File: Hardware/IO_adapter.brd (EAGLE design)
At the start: 67.3 x 41.9 mm, 23 parts, among them Y1 32Khz

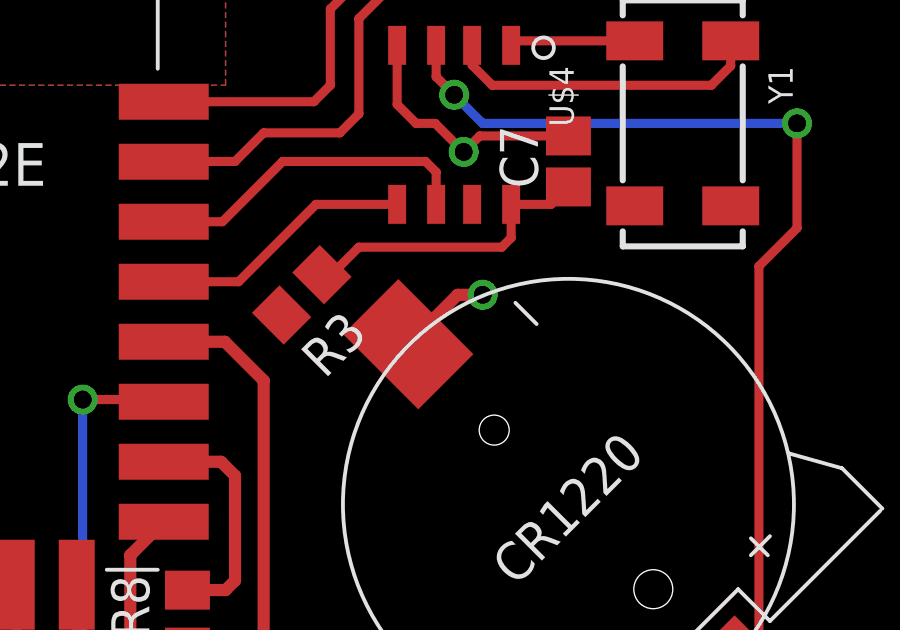
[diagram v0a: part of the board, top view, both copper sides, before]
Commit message: Revert "beginning to add a 2.2" TFT display"
This reverts commit 5a3055f75d7c66bfc0e3a1cc9d4d5180e17e1807.
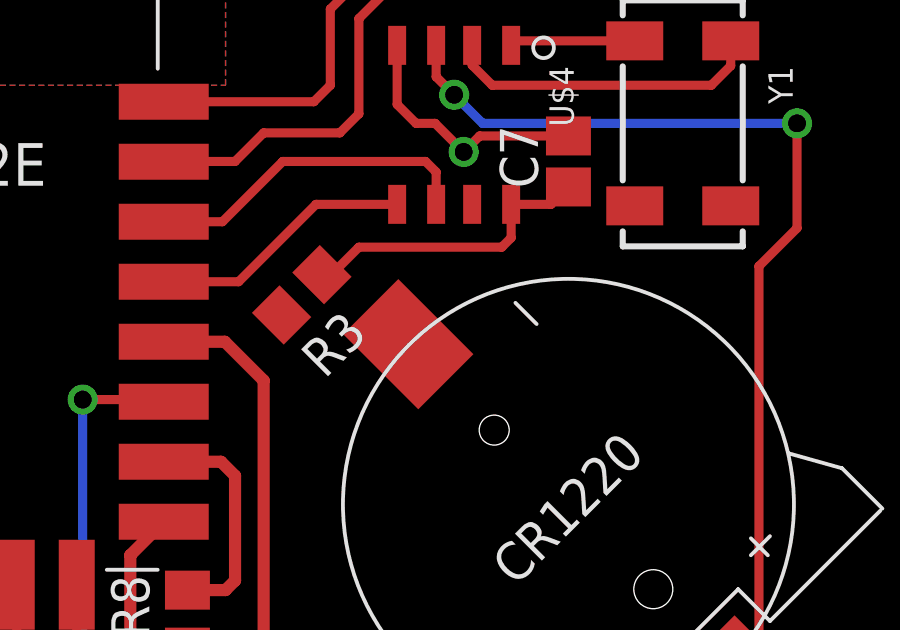
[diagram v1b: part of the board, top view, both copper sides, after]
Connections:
- net GND: no longer U$1.P-
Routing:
- net GND: track 39.9 -> 36.8 mm, vias 7 -> 6
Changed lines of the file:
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@@
 <hole x="65.195" y="1.67" drill="3"/>
 <hole x="2.005" y="1.63" drill="3"/>
-<dimension x1="0" y1="0" x2="0" y2="41.91" x3="-5.08" y3="20.955" textsize="1.778" layer="16"/>
-<dimension x1="0" y1="0" x2="67.31" y2="0" x3="33.655" y3="-2.54" textsize="1.778" layer="16"/>
 </plain>
 <attributes>
@@
 <wire x1="24.4475" y1="8.89" x2="20.85" y2="8.89" width="0.3048" layer="1"/>
 <wire x1="20.85" y1="8.89" x2="20.53" y2="8.57" width="0.3048" layer="1"/>
-<contactref element="U$1" pad="P-"/>
-<wire x1="50.54134375" y1="23.118653125" x2="52.187690625" y2="24.765" width="0.4064" layer="1"/>
-<wire x1="52.187690625" y1="24.765" x2="53.0225" y2="24.765" width="0.4064" layer="1"/>
-<via x="53.0225" y="24.765" extent="1-16" drill="0.6" shape="octagon"/>
 <wire x1="33.02" y1="6.35" x2="40.64" y2="6.35" width="0" layer="19" extent="1-1"/>
 </signal>
